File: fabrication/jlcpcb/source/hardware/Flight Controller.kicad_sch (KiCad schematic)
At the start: 0 parts

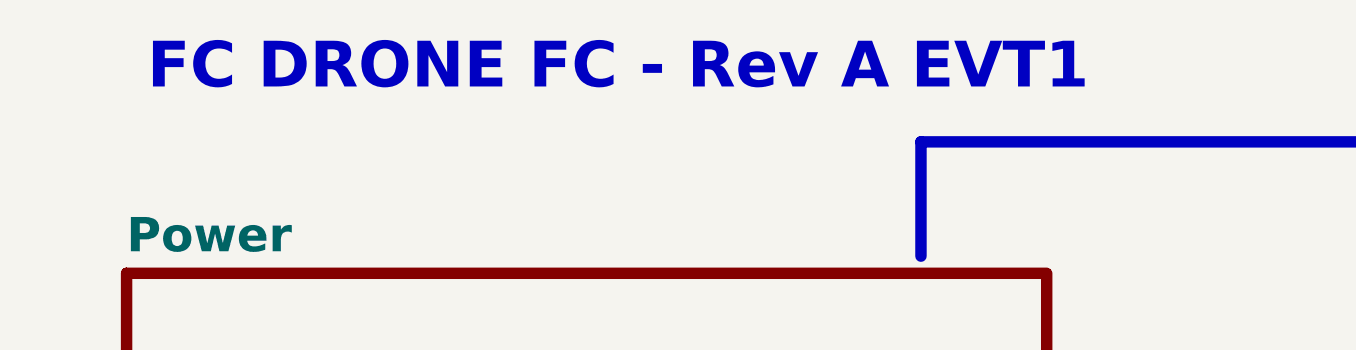
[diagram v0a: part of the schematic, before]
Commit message: docs: publish neutral engineering source, manufacturing and portfolio overview
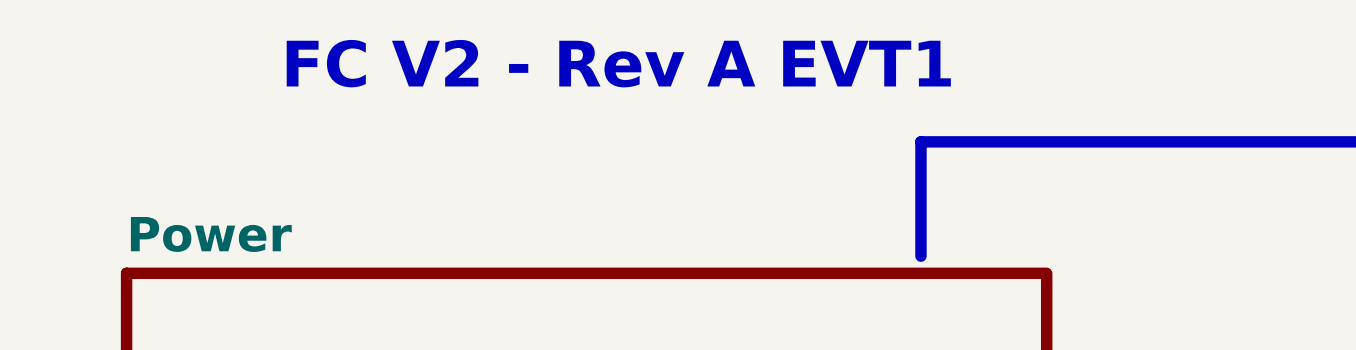
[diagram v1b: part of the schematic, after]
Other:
- note added: "FC V2 - Rev A EVT1"
- note removed: "FC DRONE FC - Rev A EVT1"
- company: FC DRONE PROJECT -> Desan Vasu
- title: FC DRONE FC -> Flight Controller V2
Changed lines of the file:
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@@
 	(paper "User" 711.2 342.9)
 	(title_block
-		(title "FC DRONE FC")
+		(title "Flight Controller V2")
 		(date "2026-09-13")
 		(rev "A")
-		(company "FC DRONE PROJECT")
+		(company "Desan Vasu")
 		(comment 1 "Derived from upstream commit 0a60da1 under CERN-OHL-S-2.0")
 		(comment 2 "POWER/OPENESC REDESIGN IMPLEMENTED - BENCH VALIDATION REQUIRED")
@@
 		)
 	)
-	(text "FC DRONE FC - Rev A EVT1"
+	(text "FC V2 - Rev A EVT1"
 		(exclude_from_sim no)
 		(at 101.6 21.59 0)
